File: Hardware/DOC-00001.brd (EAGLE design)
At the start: 22.9 x 16.5 mm, 8 parts

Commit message: Routed. Needs ground layers.
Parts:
- moved C1 13.2 mm to (2.29, 11.4), flipped to the bottom
- moved R2 11.8 mm to (2.03, 4.32), flipped to the bottom
- moved R1 6.11 mm to (2.03, 8.13), flipped to the bottom
- moved U$2 3.59 mm to (12.4, 8.26), turned to 270 degrees
- moved U$3 3.19 mm to (17.8, 8.26), turned to 270 degrees
- moved U$4 2.79 mm to (23.2, 8.26), turned to 270 degrees
- moved JP1 2.34 mm to (13.7, 2.03)
- moved U$1 2.00 mm to (5.03, 8.26), turned to 270 degrees
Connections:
- net AIN0: now also JP1.5; no longer JP1.3
- net AIN1: now also JP1.6; no longer JP1.4
- net AIN2: now also JP1.7; no longer JP1.5
- net AIN3: now also JP1.8; no longer JP1.6
- net SCL: now also JP1.3; no longer JP1.7
- net SDA: now also JP1.4; no longer JP1.8
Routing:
- net VDD: track 0.00 -> 43.8 mm, vias 0 -> 1
- net SCL: track 0.00 -> 34.8 mm, vias 0 -> 1
- net SDA: track 0.00 -> 28.6 mm, vias 0 -> 1
- net AIN0: track 0.00 -> 24.1 mm, vias 0 -> 1
- net AIN1: track 0.00 -> 15.5 mm, vias 0 -> 1
- net AIN2: track 0.00 -> 11.2 mm, vias 0 -> 1
- net AIN3: track 0.00 -> 10.9 mm, vias 0 -> 1
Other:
- board size 22.9 x 16.5 mm -> 25.4 x 12.7 mm

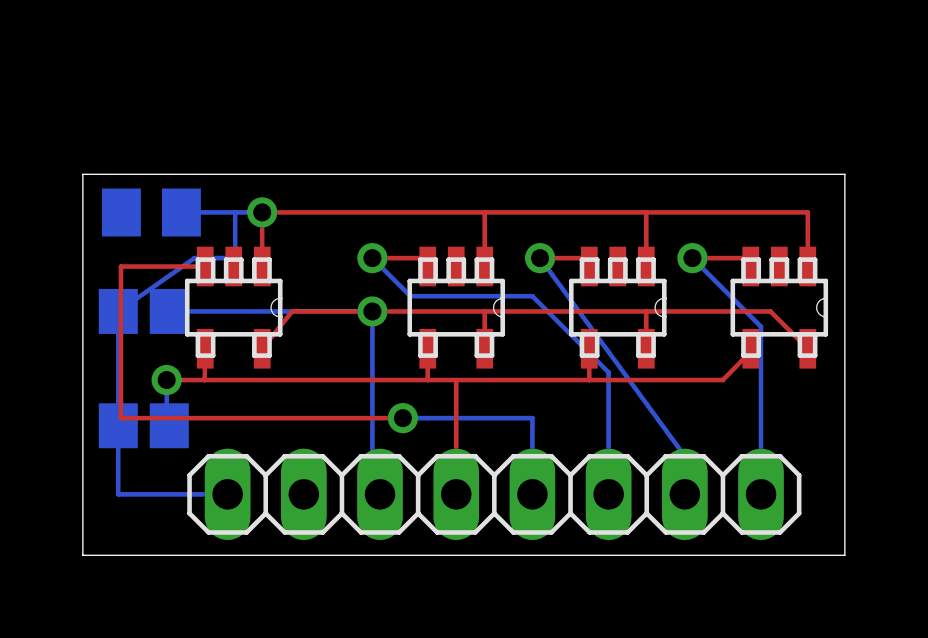
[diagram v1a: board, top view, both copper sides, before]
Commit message: Changed the PCB layout
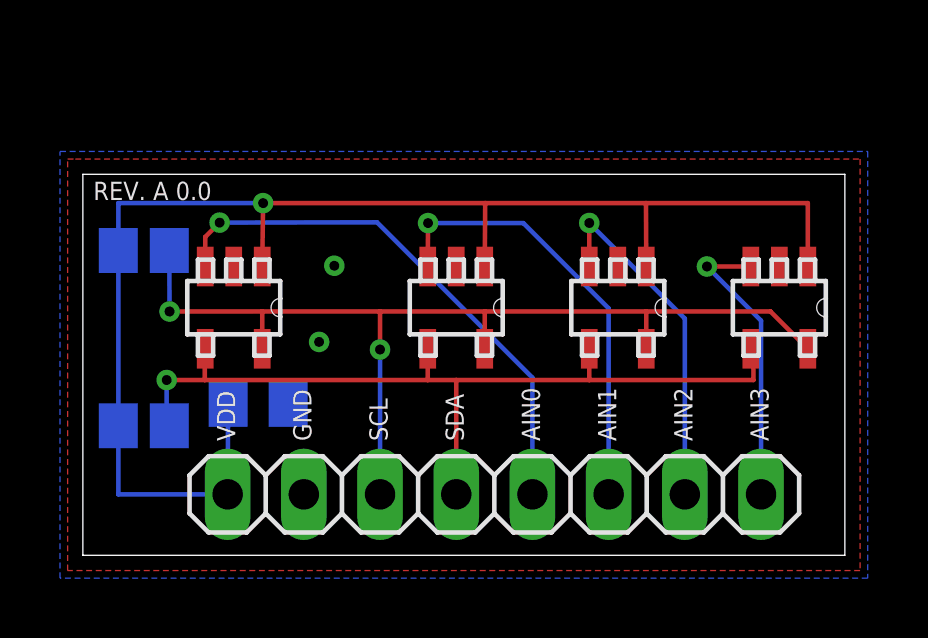
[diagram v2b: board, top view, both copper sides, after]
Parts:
- moved C1 7.28 mm to (5.84, 5.08), turned to 180 degrees
- moved R1 2.03 mm to (2.03, 10.2)
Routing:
- net AIN0: track 24.1 -> 18.1 mm
- net VDD: track 43.8 -> 47.8 mm
- net SCL: track 34.8 -> 33.7 mm, vias 1 -> 2
- net AIN3: track 10.9 -> 9.80 mm
- net AIN1: track 15.5 -> 14.8 mm
- net AIN2: track 11.2 -> 11.8 mm
- net SDA: track 28.6 -> 29.2 mm
- added copper zone on layer 1, net GND
- added copper zone on layer 16, net GND
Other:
- board text added: "AIN0"
- board text added: "AIN1"
- board text added: "AIN2"
- board text added: "AIN3"
- board text added: "GND"
- board text added: "REV. A 0.0"
- board text added: "SCL"
- board text added: "SDA"
- board text added: "VDD"
